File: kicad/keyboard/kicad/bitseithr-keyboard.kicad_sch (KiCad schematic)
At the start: 74 parts, among them P2 KEYB CONN 1

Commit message: continued work on keyboard pcb
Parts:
- MX1, MX10, MX11, MX12, MX13, MX14, MX16, MX17, MX18, MX19, MX2, MX20, MX21, MX22, MX23, MX24, MX25, MX26, MX27, MX28, MX29, MX3, MX30, MX31, MX32, MX33, MX34, MX35, MX4, MX5, MX6, MX7, MX8, MX9: footprint EasyEDA_Lib:SMD_KEYBOARD-SW -> clholm-kicad-library:MX-Hotswap-1U
- MX15: footprint EasyEDA_Lib:SMD_KEYBOARD-SW -> clholm-kicad-library:MX-Hotswap-2.25U
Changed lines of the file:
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@@
 			)
 		)
-		(property "Footprint" "EasyEDA_Lib:SMD_KEYBOARD-SW"
+		(property "Footprint" "clholm-kicad-library:MX-Hotswap-1U"
 			(at 27.305 127.635 0)
 			(effects
@@
 			)
 		)
-		(property "Footprint" "EasyEDA_Lib:SMD_KEYBOARD-SW"
+		(property "Footprint" "clholm-kicad-library:MX-Hotswap-1U"
 			(at 40.005 127.635 0)
 			(effects
@@
 			)
 		)
-		(property "Footprint" "EasyEDA_Lib:SMD_KEYBOARD-SW"
+		(property "Footprint" "clholm-kicad-library:MX-Hotswap-1U"
 			(at 78.105 127.635 0)
 			(effects
@@
 			)
 		)
-		(property "Footprint" "EasyEDA_Lib:SMD_KEYBOARD-SW"
+		(property "Footprint" "clholm-kicad-library:MX-Hotswap-1U"
 			(at 90.805 127.635 0)
 			(effects
@@
 			)
 		)
-		(property "Footprint" "EasyEDA_Lib:SMD_KEYBOARD-SW"
+		(property "Footprint" "clholm-kicad-library:MX-Hotswap-1U"
 			(at 103.505 127.635 0)
 			(effects
@@
 			)
 		)
-		(property "Footprint" "EasyEDA_Lib:SMD_KEYBOARD-SW"
+		(property "Footprint" "clholm-kicad-library:MX-Hotswap-1U"
 			(at 27.305 106.045 0)
 			(effects
@@
 			)
 		)
-		(property "Footprint" "EasyEDA_Lib:SMD_KEYBOARD-SW"
+		(property "Footprint" "clholm-kicad-library:MX-Hotswap-1U"
 			(at 40.005 106.045 0)
 			(effects
@@
 			)
 		)
-		(property "Footprint" "EasyEDA_Lib:SMD_KEYBOARD-SW"
+		(property "Footprint" "clholm-kicad-library:MX-Hotswap-1U"
 			(at 52.705 106.045 0)
 			(effects
@@
 			)
 		)
-		(property "Footprint" "EasyEDA_Lib:SMD_KEYBOARD-SW"
+		(property "Footprint" "clholm-kicad-library:MX-Hotswap-1U"
 			(at 65.405 106.045 0)
 			(effects
@@
 			)
 		)
-		(property "Footprint" "EasyEDA_Lib:SMD_KEYBOARD-SW"
+		(property "Footprint" "clholm-kicad-library:MX-Hotswap-1U"
 			(at 78.105 106.045 0)
 			(effects
@@
 			)
 		)
-		(property "Footprint" "EasyEDA_Lib:SMD_KEYBOARD-SW"
+		(property "Footprint" "clholm-kicad-library:MX-Hotswap-1U"
 			(at 90.805 106.045 0)
 			(effects
@@
 			)
 		)
-		(property "Footprint" "EasyEDA_Lib:SMD_KEYBOARD-SW"
+		(property "Footprint" "clholm-kicad-library:MX-Hotswap-1U"
 			(at 103.505 106.045 0)
 			(effects
@@
 			)
 		)
-		(property "Footprint" "EasyEDA_Lib:SMD_KEYBOARD-SW"
+		(property "Footprint" "clholm-kicad-library:MX-Hotswap-1U"
 			(at 27.305 84.455 0)
 			(effects
@@
 			)
 		)
-		(property "Footprint" "EasyEDA_Lib:SMD_KEYBOARD-SW"
+		(property "Footprint" "clholm-kicad-library:MX-Hotswap-1U"
 			(at 40.005 84.455 0)
 			(effects
@@
 			)
 		)
-		(property "Footprint" "EasyEDA_Lib:SMD_KEYBOARD-SW"
+		(property "Footprint" "clholm-kicad-library:MX-Hotswap-1U"
 			(at 78.105 84.455 0)
 			(effects
@@
 			)
 		)
-		(property "Footprint" "EasyEDA_Lib:SMD_KEYBOARD-SW"
+		(property "Footprint" "clholm-kicad-library:MX-Hotswap-1U"
 			(at 90.805 84.455 0)
 			(effects
@@
 			)
 		)
-		(property "Footprint" "EasyEDA_Lib:SMD_KEYBOARD-SW"
+		(property "Footprint" "clholm-kicad-library:MX-Hotswap-1U"
 			(at 103.505 84.455 0)
 			(effects
@@
 			)
 		)
-		(property "Footprint" "EasyEDA_Lib:SMD_KEYBOARD-SW"
+		(property "Footprint" "clholm-kicad-library:MX-Hotswap-1U"
 			(at 27.305 149.225 0)
 			(effects
@@
 			)
 		)
-		(property "Footprint" "EasyEDA_Lib:SMD_KEYBOARD-SW"
+		(property "Footprint" "clholm-kicad-library:MX-Hotswap-1U"
 			(at 40.005 149.225 0)
 			(effects
@@
 			)
 		)
-		(property "Footprint" "EasyEDA_Lib:SMD_KEYBOARD-SW"
+		(property "Footprint" "clholm-kicad-library:MX-Hotswap-1U"
 			(at 52.705 149.225 0)
 			(effects
@@
 			)
 		)
-		(property "Footprint" "EasyEDA_Lib:SMD_KEYBOARD-SW"
+		(property "Footprint" "clholm-kicad-library:MX-Hotswap-1U"
 			(at 65.405 149.225 0)
 			(effects
@@
 			)
 		)
-		(property "Footprint" "EasyEDA_Lib:SMD_KEYBOARD-SW"
+		(property "Footprint" "clholm-kicad-library:MX-Hotswap-1U"
 			(at 78.105 149.225 0)
 			(effects
@@
 			)
 		)
-		(property "Footprint" "EasyEDA_Lib:SMD_KEYBOARD-SW"
+		(property "Footprint" "clholm-kicad-library:MX-Hotswap-1U"
 			(at 90.805 149.225 0)
 			(effects
@@
 			)
 		)
-		(property "Footprint" "EasyEDA_Lib:SMD_KEYBOARD-SW"
+		(property "Footprint" "clholm-kicad-library:MX-Hotswap-1U"
 			(at 103.505 149.225 0)
 			(effects
@@
 			)
 		)
-		(property "Footprint" "EasyEDA_Lib:SMD_KEYBOARD-SW"
+		(property "Footprint" "clholm-kicad-library:MX-Hotswap-1U"
 			(at 27.305 62.865 0)
 			(effects
@@
 			)
 		)
-		(property "Footprint" "EasyEDA_Lib:SMD_KEYBOARD-SW"
+		(property "Footprint" "clholm-kicad-library:MX-Hotswap-1U"
 			(at 52.705 62.865 0)
 			(effects
@@
 			)
 		)
-		(property "Footprint" "EasyEDA_Lib:SMD_KEYBOARD-SW"
+		(property "Footprint" "clholm-kicad-library:MX-Hotswap-1U"
 			(at 78.105 62.865 0)
 			(effects
@@
 			)
 		)
-		(property "Footprint" "EasyEDA_Lib:SMD_KEYBOARD-SW"
+		(property "Footprint" "clholm-kicad-library:MX-Hotswap-1U"
 			(at 103.505 62.865 0)
 			(effects
@@
 			)
 		)
-		(property "Footprint" "EasyEDA_Lib:SMD_KEYBOARD-SW"
+		(property "Footprint" "clholm-kicad-library:MX-Hotswap-2.25U"
 			(at 65.405 170.815 0)
 			(effects
@@
 			)
 		)
-		(property "Footprint" "EasyEDA_Lib:SMD_KEYBOARD-SW"
+		(property "Footprint" "clholm-kicad-library:MX-Hotswap-1U"
 			(at 146.685 106.045 0)
 			(effects
@@
 			)
 		)
-		(property "Footprint" "EasyEDA_Lib:SMD_KEYBOARD-SW"
+		(property "Footprint" "clholm-kicad-library:MX-Hotswap-1U"
 			(at 146.685 84.455 0)
 			(effects
@@
 			)
 		)
-		(property "Footprint" "EasyEDA_Lib:SMD_KEYBOARD-SW"
+		(property "Footprint" "clholm-kicad-library:MX-Hotswap-1U"
 			(at 116.205 106.045 0)
 			(effects
@@
 			)
 		)
-		(property "Footprint" "EasyEDA_Lib:SMD_KEYBOARD-SW"
+		(property "Footprint" "clholm-kicad-library:MX-Hotswap-1U"
 			(at 116.205 149.225 0)
 			(effects
@@
 			)
 		)
-		(property "Footprint" "EasyEDA_Lib:SMD_KEYBOARD-SW"
+		(property "Footprint" "clholm-kicad-library:MX-Hotswap-1U"
 			(at 146.685 127.635 0)
 			(effects
@@
 			)
 		)
-		(property "Footprint" "EasyEDA_Lib:SMD_KEYBOARD-SW"
+		(property "Footprint" "clholm-kicad-library:MX-Hotswap-1U"
 			(at 146.685 149.225 0)
 			(effects

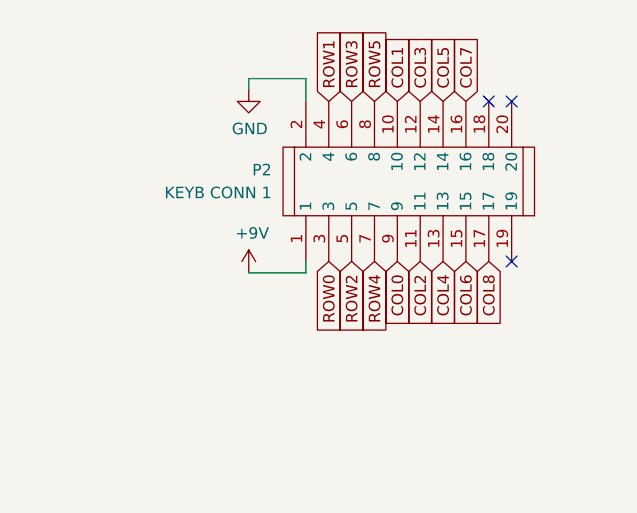
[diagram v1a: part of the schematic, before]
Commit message: updated keyboard connector pinout for better trace routing (hopefully)
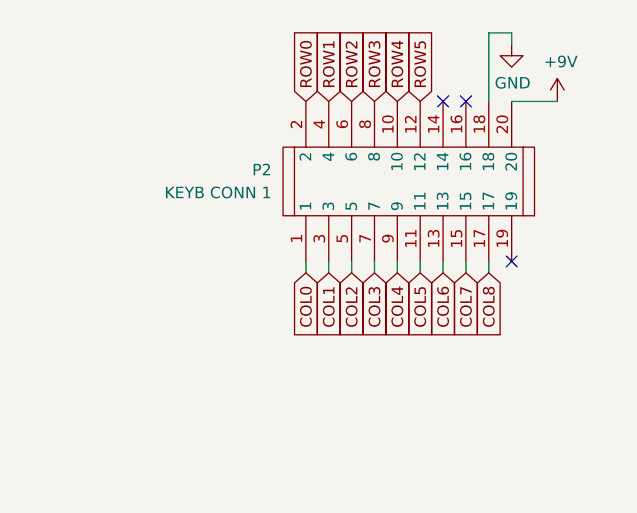
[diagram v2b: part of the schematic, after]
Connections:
- net +9V: now also P2.20; no longer P2.1
- net COL0: now also P2.1; no longer P2.9
- net COL1: now also P2.3; no longer P2.10
- net COL2: now also P2.5; no longer P2.11
- net COL3: now also P2.7; no longer P2.12
- net COL4: now also P2.9; no longer P2.13
- net COL5: now also P2.11; no longer P2.14
- net COL6: now also P2.13; no longer P2.15
- net COL7: now also P2.15; no longer P2.16
- net GND: now also P2.18; no longer P2.2
- net ROW0: now also P2.2; no longer P2.3
- net ROW2: now also P2.6; no longer P2.5
- net ROW3: now also P2.8; no longer P2.6
- net ROW4: now also P2.10; no longer P2.7
- net ROW5: now also P2.12; no longer P2.8
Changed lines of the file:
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@@
 	)
 	(no_connect
-		(at 242.57 31.75)
+		(at 234.95 31.75)
 	)
 	(no_connect
-		(at 240.03 31.75)
+		(at 237.49 31.75)
 	)
 	(no_connect
@@
 	(wire
 		(pts
-			(xy 219.71 50.8) (xy 213.36 50.8)
+			(xy 242.57 31.75) (xy 247.65 31.75)
 		)
 		(stroke
@@
 	(wire
 		(pts
-			(xy 213.36 29.21) (xy 219.71 29.21)
+			(xy 38.1 138.43) (xy 41.91 138.43)
 		)
 		(stroke
@@
 	(wire
 		(pts
-			(xy 38.1 138.43) (xy 41.91 138.43)
+			(xy 240.03 24.13) (xy 242.57 24.13)
+		)
+		(stroke
+			(width 0)
+			(type default)
+		)
+	)
+	(wire
+		(pts
+			(xy 242.57 25.4) (xy 242.57 24.13)
 		)
 		(stroke
@@
 	(wire
 		(pts
-			(xy 213.36 30.48) (xy 213.36 29.21)
+			(xy 240.03 49.53) (xy 240.03 50.8)
 		)
 		(stroke
@@
 	(wire
 		(pts
+			(xy 229.87 49.53) (xy 229.87 50.8)
+		)
+		(stroke
+			(width 0)
+			(type default)
+		)
+	)
+	(wire
+		(pts
 			(xy 110.49 125.73) (xy 110.49 147.32)
 		)
@@
 	(wire
 		(pts
+			(xy 232.41 49.53) (xy 232.41 50.8)
+		)
+		(stroke
+			(width 0)
+			(type default)
+		)
+	)
+	(wire
+		(pts
 			(xy 72.39 104.14) (xy 72.39 147.32)
 		)
@@
 	(wire
 		(pts
-			(xy 240.03 113.03) (xy 240.03 114.3)
+			(xy 234.95 49.53) (xy 234.95 50.8)
 		)
 		(stroke
@@
 	(wire
 		(pts
-			(xy 219.71 29.21) (xy 219.71 31.75)
+			(xy 240.03 113.03) (xy 240.03 114.3)
 		)
 		(stroke
@@
 	(wire
 		(pts
+			(xy 227.33 49.53) (xy 227.33 50.8)
+		)
+		(stroke
+			(width 0)
+			(type default)
+		)
+	)
+	(wire
+		(pts
 			(xy 46.99 82.55) (xy 46.99 104.14)
 		)
@@
 	(wire
 		(pts
+			(xy 222.25 49.53) (xy 222.25 50.8)
+		)
+		(stroke
+			(width 0)
+			(type default)
+		)
+	)
+	(wire
+		(pts
 			(xy 236.22 102.87) (xy 240.03 102.87)
 		)
@@
 	(wire
 		(pts
+			(xy 224.79 49.53) (xy 224.79 50.8)
+		)
+		(stroke
+			(width 0)
+			(type default)
+		)
+	)
+	(wire
+		(pts
 			(xy 118.11 95.25) (xy 161.29 95.25)
 		)
@@
 	(wire
 		(pts
+			(xy 237.49 49.53) (xy 237.49 50.8)
+		)
+		(stroke
+			(width 0)
+			(type default)
+		)
+	)
+	(wire
+		(pts
+			(xy 240.03 31.75) (xy 240.03 24.13)
+		)
+		(stroke
+			(width 0)
+			(type default)
+		)
+	)
+	(wire
+		(pts
 			(xy 135.89 53.34) (xy 135.89 104.14)
 		)
@@
 	(global_label "COL6"
 		(shape input)
-		(at 237.49 49.53 270)
+		(at 234.95 50.8 270)
 		(effects
 			(font
@@
 		)
 		(property "Intersheetrefs" "${INTERSHEET_REFS}"
-			(at 237.49 49.53 0)
+			(at 234.95 50.8 0)
 			(effects
 				(font
@@
 	(global_label "COL5"
 		(shape input)
-		(at 234.95 31.75 90)
+		(at 232.41 50.8 270)
 		(effects
 			(font
 				(size 1.27 1.27)
 			)
-			(justify left)
+			(justify right)
 		)
 		(property "Intersheetrefs" "${INTERSHEET_REFS}"
-			(at 234.95 31.75 0)
+			(at 232.41 50.8 0)
 			(effects
 				(font
@@
 	(global_label "ROW4"
 		(shape input)
-		(at 227.33 49.53 270)
+		(at 229.87 31.75 90)
 		(effects
 			(font
 				(size 1.27 1.27)
 			)
-			(justify right)
+			(justify left)
 		)
 		(property "Intersheetrefs" "${INTERSHEET_REFS}"
-			(at 227.33 49.53 90)
+			(at 229.87 31.75 90)
 			(effects
 				(font
@@
 	(global_label "COL8"
 		(shape input)
-		(at 240.03 49.53 270)
+		(at 240.03 50.8 270)
 		(effects
 			(font
@@
 		)
 		(property "Intersheetrefs" "${INTERSHEET_REFS}"
-			(at 240.03 49.53 0)
+			(at 240.03 50.8 0)
 			(effects
 				(font
@@
 	(global_label "ROW0"
 		(shape input)
-		(at 222.25 49.53 270)
+		(at 219.71 31.75 90)
 		(effects
 			(font
 				(size 1.27 1.27)
 			)
-			(justify right)
+			(justify left)
 		)
 		(property "Intersheetrefs" "${INTERSHEET_REFS}"
-			(at 222.25 49.53 90)
+			(at 219.71 31.75 90)
 			(effects
 				(font
@@
 	(global_label "COL1"
 		(shape input)
-		(at 229.87 31.75 90)
+		(at 222.25 50.8 270)
 		(effects
 			(font
 				(size 1.27 1.27)
 			)
-			(justify left)
+			(justify right)
 		)
 		(property "Intersheetrefs" "${INTERSHEET_REFS}"
-			(at 229.87 31.75 0)
+			(at 222.25 50.8 0)
 			(effects
 				(font
@@
 	(global_label "ROW5"
 		(shape input)
-		(at 227.33 31.75 90)
+		(at 232.41 31.75 90)
 		(effects
 			(font
@@
 		)
 		(property "Intersheetrefs" "${INTERSHEET_REFS}"
-			(at 227.33 31.75 90)
+			(at 232.41 31.75 90)
 			(effects
 				(font
@@
 	(global_label "COL2"
 		(shape input)
-		(at 232.41 49.53 270)
+		(at 224.79 50.8 270)
 		(effects
 			(font
@@
 		)
 		(property "Intersheetrefs" "${INTERSHEET_REFS}"
-			(at 232.41 49.53 0)
+			(at 224.79 50.8 0)
 			(effects
 				(font
@@
 	(global_label "COL4"
 		(shape input)
-		(at 234.95 49.53 270)
+		(at 229.87 50.8 270)
 		(effects
 			(font
@@
 		)
 		(property "Intersheetrefs" "${INTERSHEET_REFS}"
-			(at 234.95 49.53 0)
+			(at 229.87 50.8 0)
 			(effects
 				(font
@@
 	(global_label "COL7"
 		(shape input)
-		(at 237.49 31.75 90)
+		(at 237.49 50.8 270)
 		(effects
 			(font
 				(size 1.27 1.27)
 			)
-			(justify left)
+			(justify right)
 		)
 		(property "Intersheetrefs" "${INTERSHEET_REFS}"
-			(at 237.49 31.75 0)
+			(at 237.49 50.8 0)
 			(effects
 				(font
@@
 	(global_label "ROW3"
 		(shape input)
-		(at 224.79 31.75 90)
+		(at 227.33 31.75 90)
 		(effects
 			(font
@@
 		)
 		(property "Intersheetrefs" "${INTERSHEET_REFS}"
-			(at 224.79 31.75 90)
+			(at 227.33 31.75 90)
 			(effects
 				(font
@@
 	(global_label "COL0"
 		(shape input)
-		(at 229.87 49.53 270)
+		(at 219.71 50.8 270)
 		(effects
 			(font
@@
 		)
 		(property "Intersheetrefs" "${INTERSHEET_REFS}"
-			(at 229.87 49.53 0)
+			(at 219.71 50.8 0)
 			(effects
 				(font
@@
 	(global_label "COL3"
 		(shape input)
-		(at 232.41 31.75 90)
+		(at 227.33 50.8 270)
 		(effects
 			(font
 				(size 1.27 1.27)
 			)
-			(justify left)
+			(justify right)
 		)
 		(property "Intersheetrefs" "${INTERSHEET_REFS}"
-			(at 232.41 31.75 0)
+			(at 227.33 50.8 0)
 			(effects
 				(font
@@
 	(global_label "ROW2"
 		(shape input)
-		(at 224.79 49.53 270)
+		(at 224.79 31.75 90)
 		(effects
 			(font
 				(size 1.27 1.27)
 			)
-			(justify right)
+			(justify left)
 		)
 		(property "Intersheetrefs" "${INTERSHEET_REFS}"
-			(at 224.79 49.53 90)
+			(at 224.79 31.75 90)
 			(effects
 				(font
@@
 	(symbol
 		(lib_id "power:+9V")
-		(at 213.36 50.8 0)
+		(at 247.65 31.75 0)
 		(unit 1)
 		(exclude_from_sim no)
@@
 		(dnp no)
 		(property "Reference" "#PWR056"
-			(at 213.36 54.61 0)
+			(at 247.65 35.56 0)
 			(effects
 				(font
@@
 		)
 		(property "Value" "+9V"
-			(at 213.741 46.4058 0)
+			(at 248.031 27.3558 0)
 			(effects
 				(font
@@
 		)
 		(property "Footprint" ""
-			(at 213.36 50.8 0)
+			(at 247.65 31.75 0)
 			(effects
 				(font
@@
 		)
 		(property "Datasheet" ""
-			(at 213.36 50.8 0)
+			(at 247.65 31.75 0)
 			(effects
 				(font
@@
 		)
 		(property "Description" ""
-			(at 213.36 50.8 0)
+			(at 247.65 31.75 0)
 			(effects
 				(font
@@
 	(symbol
 		(lib_id "power:GND")
-		(at 213.36 30.48 0)
+		(at 242.57 25.4 0)
 		(unit 1)
 		(exclude_from_sim no)
@@
 		(dnp no)
 		(property "Reference" "#PWR055"
-			(at 213.36 36.83 0)
+			(at 242.57 31.75 0)
 			(effects
 				(font
@@
 		)
 		(property "Value" "GND"
-			(at 213.4743 34.8044 0)
+			(at 242.6843 29.7244 0)
 			(effects
 				(font
@@
 		)
 		(property "Footprint" ""
-			(at 213.36 30.48 0)
+			(at 242.57 25.4 0)
 			(effects
 				(font
@@
 		)
 		(property "Datasheet" ""
-			(at 213.36 30.48 0)
+			(at 242.57 25.4 0)
 			(effects
 				(font
@@
 		)
 		(property "Description" "Power symbol creates a global label with name \"GND\" , ground"
-			(at 213.36 30.48 0)
+			(at 242.57 25.4 0)
 			(effects
 				(font
